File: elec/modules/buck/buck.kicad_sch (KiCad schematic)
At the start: 18 parts, among them J1 Conn_01x08, J2 Conn_01x08, U2 TPS5430DDAG4, U3 TPS5430DDAG4

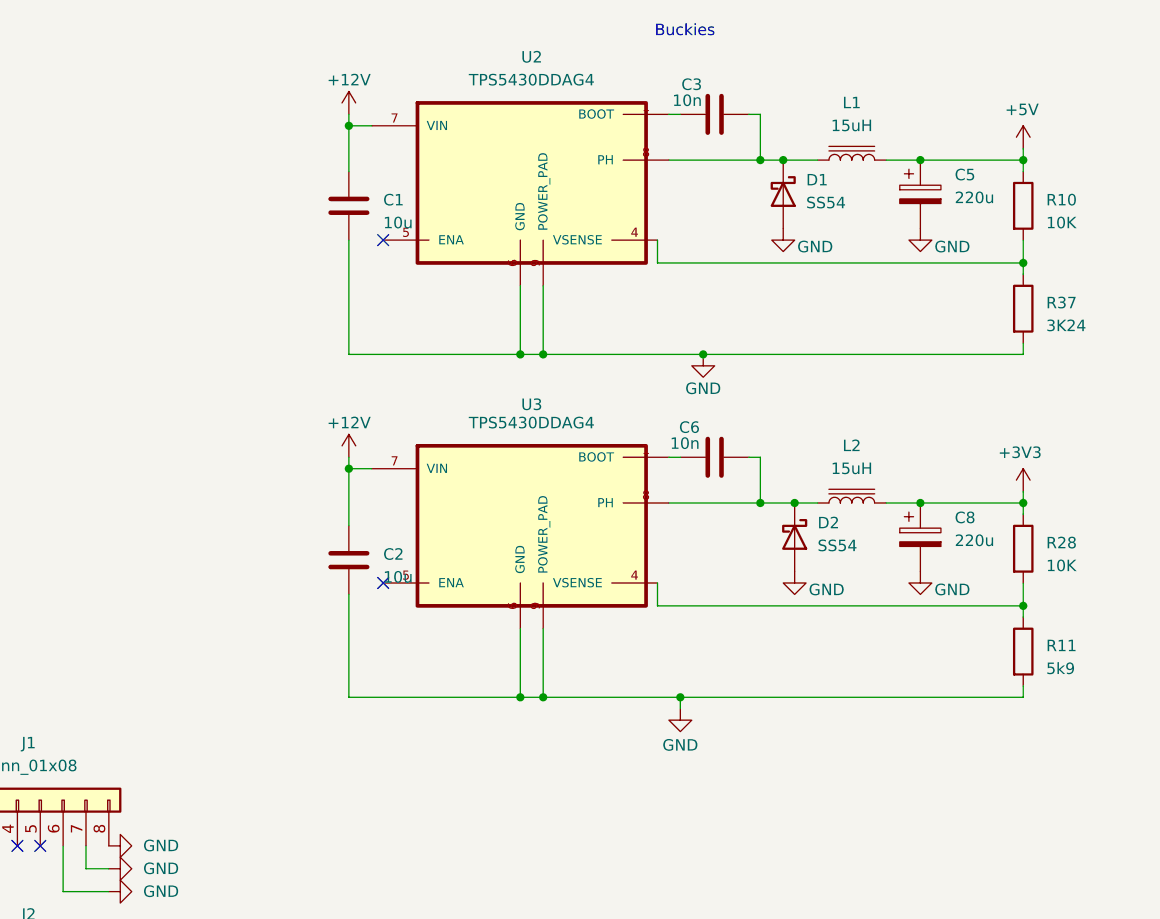
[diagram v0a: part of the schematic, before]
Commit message: Finished slaving avay buck done +PCBA
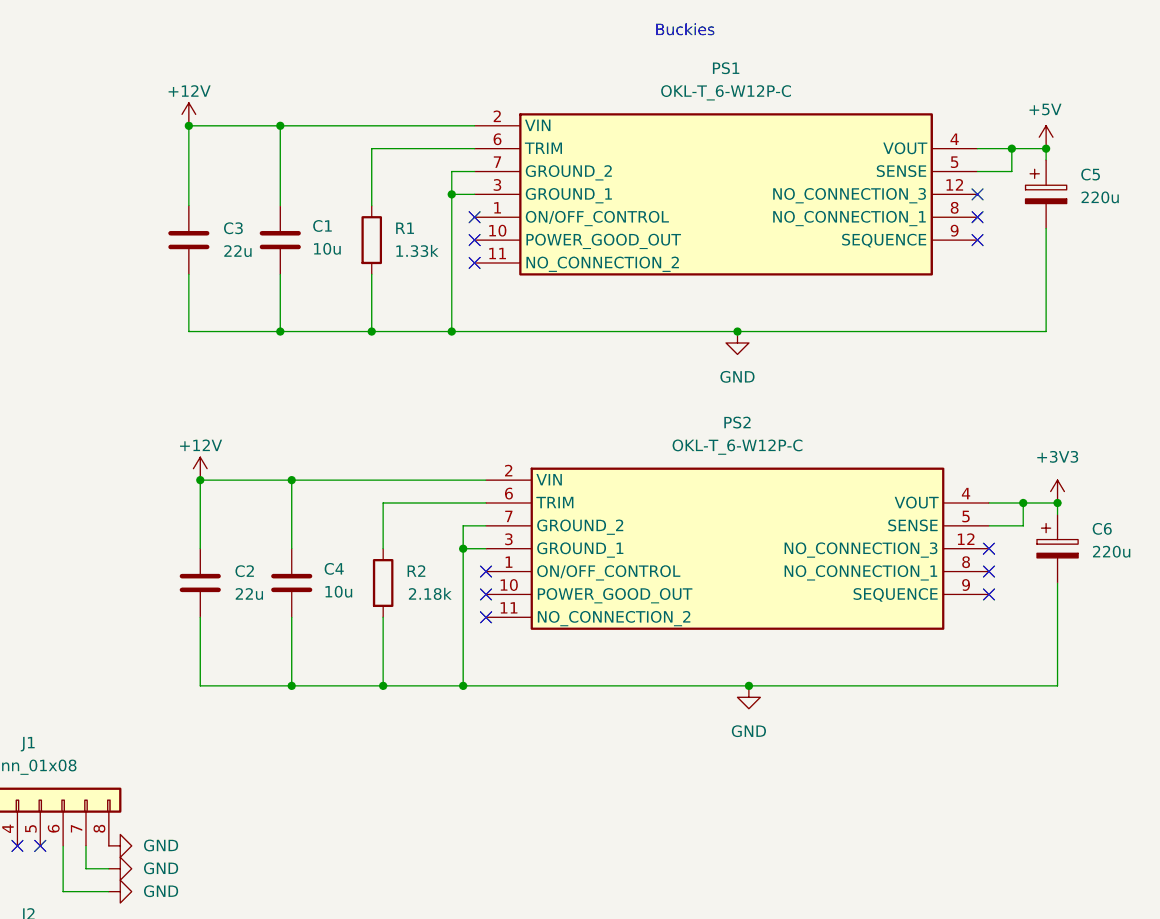
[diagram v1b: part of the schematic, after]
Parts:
- removed C6: 10n, Capacitor_SMD:C_0603_1608Metric, symbol Device:C
- removed C8: 220u, Capacitor_Tantalum_SMD:CP_EIA-7343-15_Kemet-W_HandSolder, symbol Device:C_Polarized
- removed D1, D2: SS54, Buckies:DIOM5025X220N, symbol Diode:B340
- removed L1, L2: 15uH, Buckies:0630 One Piece Inductor, symbol Device:L_Iron
- removed R10, R28: 10K, Resistor_SMD:R_0603_1608Metric, symbol Device:R
- removed R11: 5k9, Resistor_SMD:R_0603_1608Metric, symbol Device:R
- removed R37: 3K24, Resistor_SMD:R_0603_1608Metric, symbol Device:R
- removed U2, U3: TPS5430DDAG4, Buckies:TI_SO-PowerPAD-8, symbol tps5430(buckie):TPS5430DDAG4
- added C4: 10u, Capacitor_SMD:C_0603_1608Metric, symbol Device:C
- added C6: 220u, Capacitor_Tantalum_SMD:CP_EIA-7343-15_Kemet-W_HandSolder, symbol Device:C_Polarized
- added PS1, PS2: OKL-T_6-W12P-C, Buck:OKLT6W12PC, symbol OKL-T/6-W12P-C:OKL-T_6-W12P-C
- added R1: 1.33k, Resistor_SMD:R_0603_1608Metric, symbol Device:R
- added R2: 2.18k, Resistor_SMD:R_0603_1608Metric, symbol Device:R
- C2: value 10u -> 22u
- C3: value 10n -> 22u
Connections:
- net +12V: now also C3.1, C4.1, PS1.2 (VIN), PS2.2 (VIN)
- net +3V3: now also C6.1, PS2.4 (VOUT), PS2.5 (SENSE)
- net +5V: now also PS1.4 (VOUT), PS1.5 (SENSE)
- net GND: now also C3.2, C4.2, C6.2, PS1.3 (GROUND_1), PS1.7 (GROUND_2), PS2.3 (GROUND_1), PS2.7 (GROUND_2), R1.2, R2.2
- new net: PS2.6 (TRIM), R2.1
- new net: PS1.6 (TRIM), R1.1
- no-connect marks 6 -> 16
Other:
- moved on the sheet: C1, C5

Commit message: changed buck footprint
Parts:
- PS1, PS2: footprint Buck:OKLT6W12PC -> Buck:MURATA_OKL-T-6-W12
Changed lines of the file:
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@@
 			)
 		)
-		(property "Footprint" "Buck:OKLT6W12PC"
+		(property "Footprint" "Buck:MURATA_OKL-T-6-W12"
 			(at 156.21 195.25 0)
 			(effects
@@
 			)
 		)
-		(property "Footprint" "Buck:OKLT6W12PC"
+		(property "Footprint" "Buck:MURATA_OKL-T-6-W12"
 			(at 154.94 155.88 0)
 			(effects

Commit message: stuff
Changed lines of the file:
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@@
 	(generator_version "9.0")
 	(paper "A4")
+	(rectangle
+		(start 237.49 90.17)
+		(end 259.715 98.425)
+		(stroke
+			(width 0)
+			(type default)
+		)
+		(fill
+			(type none)
+		)
+	)
+	(rectangle
+		(start 214.63 88.9)
+		(end 232.41 99.06)
+		(stroke
+			(width 0)
+			(type default)
+		)
+		(fill
+			(type none)
+		)
+	)
+	(rectangle
+		(start 209.55 83.82)
+		(end 271.78 119.38)
+		(stroke
+			(width 0)
+			(type default)
+		)
+		(fill
+			(type none)
+		)
+	)
+	(rectangle
+		(start 217.17 111.76)
+		(end 264.16 114.3)
+		(stroke
+			(width 0)
+			(type default)
+		)
+		(fill
+			(type none)
+		)
+	)
 	(text "Buckies"
 		(exclude_from_sim no)

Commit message: Revert "wdicajdfkj,"
This reverts commit e49fd520bb1bff58c9ec61a88596577cb6380b2a.
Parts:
- removed J1, J2: Conn_01x08, Pinheaders:PinHeader_1x08_P2.54mm_Vertical, symbol Connector_Generic:Conn_01x08
- added J1: Conn_01x12, Connector_JST:JST_XH_B12B-XH-AM_1x12_P2.50mm_Vertical, symbol Connector_Generic:Conn_01x12
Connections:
- net +12V: now also J1.4 (Pin_4), J1.5 (Pin_5), J1.6 (Pin_6)
- net +3V3: now also J1.10 (Pin_10), J1.11 (Pin_11), J1.12 (Pin_12)
- net +5V: now also J1.1 (Pin_1), J1.2 (Pin_2), J1.3 (Pin_3)
- net GND: now also J1.7 (Pin_7), J1.8 (Pin_8), J1.9 (Pin_9)
- no-connect marks 16 -> 12

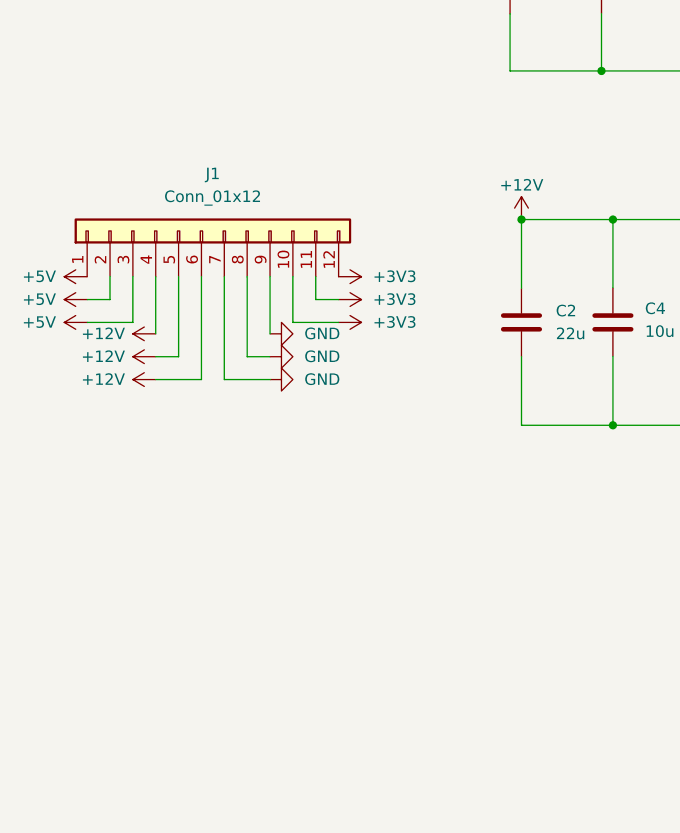
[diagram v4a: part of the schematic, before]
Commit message: Revert "did a bit of buck"
This reverts commit f549f5fa1dabaa1ceabc4869307f1601dc61308a.
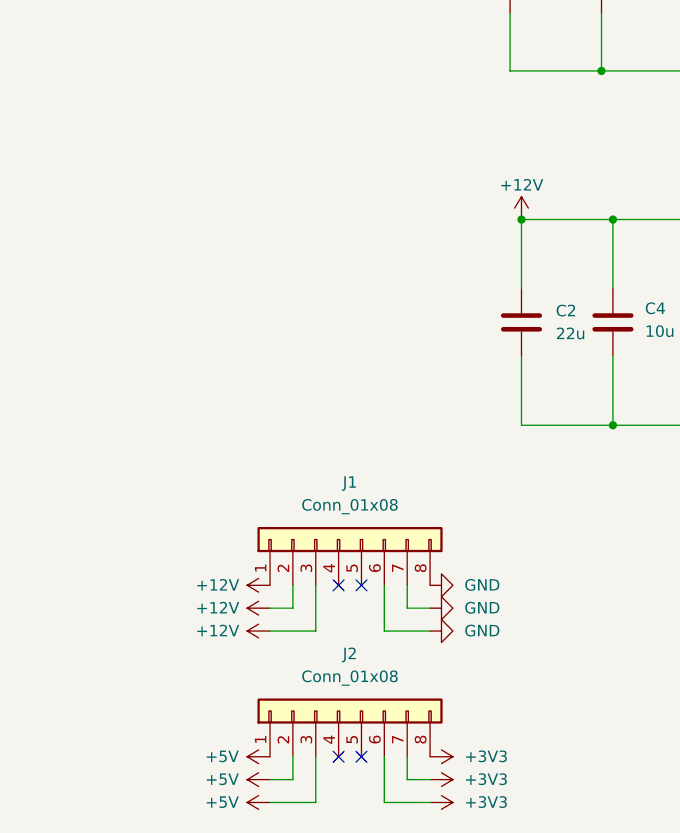
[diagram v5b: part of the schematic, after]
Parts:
- removed J1: Conn_01x12, Connector_JST:JST_XH_B12B-XH-AM_1x12_P2.50mm_Vertical, symbol Connector_Generic:Conn_01x12
- added J1, J2: Conn_01x08, Pinheaders:PinHeader_1x08_P2.54mm_Vertical, symbol Connector_Generic:Conn_01x08
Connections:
- net +12V: now also J1.1 (Pin_1), J1.2 (Pin_2), J1.3 (Pin_3)
- net +3V3: now also J2.6 (Pin_6), J2.7 (Pin_7), J2.8 (Pin_8)
- net +5V: now also J2.1 (Pin_1), J2.2 (Pin_2), J2.3 (Pin_3)
- net GND: now also J1.6 (Pin_6), J1.7 (Pin_7), J1.8 (Pin_8)
- no-connect marks 12 -> 16

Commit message: unfucked bucks and touched on l1/2
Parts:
- added D1, D2: SS54, Buck:DIOM5025X220N, symbol Diode:B340
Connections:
- net +3V3: now also D2.1 (K); no longer C6.1, PS2.4 (VOUT), PS2.5 (SENSE)
- net +5V: now also D1.1 (K); no longer C5.1, PS1.4 (VOUT), PS1.5 (SENSE)
- new net: C5.1, D1.2 (A), PS1.4 (VOUT), PS1.5 (SENSE)
- new net: C6.1, D2.2 (A), PS2.4 (VOUT), PS2.5 (SENSE)
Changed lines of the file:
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@@
 	(generator_version "9.0")
 	(paper "A4")
-	(rectangle
-		(start 237.49 90.17)
-		(end 259.715 98.425)
-		(stroke
-			(width 0)
-			(type default)
-		)
-		(fill
-			(type none)
-		)
-	)
-	(rectangle
-		(start 214.63 88.9)
-		(end 232.41 99.06)
-		(stroke
-			(width 0)
-			(type default)
-		)
-		(fill
-			(type none)
-		)
-	)
-	(rectangle
-		(start 209.55 83.82)
-		(end 271.78 119.38)
-		(stroke
-			(width 0)
-			(type default)
-		)
-		(fill
-			(type none)
-		)
-	)
-	(rectangle
-		(start 217.17 111.76)
-		(end 264.16 114.3)
-		(stroke
-			(width 0)
-			(type default)
-		)
-		(fill
-			(type none)
-		)
-	)
 	(text "Buckies"
 		(exclude_from_sim no)
@@
 	(wire
 		(pts
+			(xy 179.07 62.23) (xy 177.8 62.23)
+		)
+		(stroke
+			(width 0)
+			(type default)
+		)
+	)
+	(wire
+		(pts
 			(xy 81.28 59.69) (xy 102.87 59.69)
 		)
@@
 	(wire
 		(pts
+			(xy 179.07 101.6) (xy 177.8 101.6)
+		)
+		(stroke
+			(width 0)
+			(type default)
+		)
+	)
+	(wire
+		(pts
 			(xy 162.56 64.77) (xy 162.56 62.23)
 		)
@@
 	(wire
 		(pts
+			(xy 170.18 101.6) (xy 167.64 101.6)
+		)
+		(stroke
+			(width 0)
+			(type default)
+		)
+	)
+	(wire
+		(pts
 			(xy 46.99 158.75) (xy 46.99 161.29)
 		)
@@
 		(pts
 			(xy 104.14 104.14) (xy 101.6 104.14)
+		)
+		(stroke
+			(width 0)
+			(type default)
+		)
+	)
+	(wire
+		(pts
+			(xy 170.18 62.23) (xy 166.37 62.23)
 		)
 		(stroke
@@
 	(symbol
 		(lib_id "power:+3V3")
-		(at 167.64 101.6 0)
+		(at 179.07 101.6 270)
 		(unit 1)
 		(exclude_from_sim no)
@@
 		(fields_autoplaced yes)
 		(property "Reference" "#PWR012"
-			(at 167.64 105.41 0)
+			(at 175.26 101.6 0)
 			(effects
 				(font
@@
 		)
 		(property "Value" "+3V3"
-			(at 167.64 96.52 0)
-			(effects
-				(font
-					(size 1.27 1.27)
-				)
+			(at 182.88 101.5999 90)
+			(effects
+				(font
+					(size 1.27 1.27)
+				)
+				(justify left)
 			)
 		)
 		(property "Footprint" ""
-			(at 167.64 101.6 0)
+			(at 179.07 101.6 0)
 			(effects
 				(font
@@
 		)
 		(property "Datasheet" ""
-			(at 167.64 101.6 0)
+			(at 179.07 101.6 0)
 			(effects
 				(font
@@
 		)
 		(property "Description" "Power symbol creates a global label with name \"+3V3\""
-			(at 167.64 101.6 0)
+			(at 179.07 101.6 0)
 			(effects
 				(font
@@
 	)
 	(symbol
+		(lib_id "Diode:B340")
+		(at 173.99 62.23 180)
+		(unit 1)
+		(exclude_from_sim no)
+		(in_bom yes)
+		(on_board yes)
+		(dnp no)
+		(fields_autoplaced yes)
+		(property "Reference" "D1"
+			(at 174.3075 55.88 0)
+			(effects
+				(font
+					(size 1.27 1.27)
+				)
+			)
+		)
+		(property "Value" "SS54"
+			(at 174.3075 58.42 0)
+			(effects
+				(font
+					(size 1.27 1.27)
+				)
+			)
+		)
+		(property "Footprint" "Buck:DIOM5025X220N"
+			(at 173.99 57.785 0)
+			(effects
+				(font
+					(size 1.27 1.27)
+				)
+				(hide yes)
+			)
+		)
+		(property "Datasheet" "http://www.jameco.com/Jameco/Products/ProdDS/1538777.pdf"
+			(at 173.99 62.23 0)
+			(effects
+				(font
+					(size 1.27 1.27)
+				)
+				(hide yes)
+			)
+		)
+		(property "Description" ""
+			(at 173.99 62.23 0)
+			(effects
+				(font
+					(size 1.27 1.27)
+				)
+				(hide yes)
+			)
+		)
+		(pin "1"
+		)
+		(pin "2"
+		)
+		(instances
+			(project "buck"
+				(path "/b0c14512-e8a3-4c13-88d8-be98af63a21a"
+					(reference "D1")
+					(unit 1)
+				)
+			)
+		)
+	)
+	(symbol
 		(lib_id "power:+3V3")
 		(at 62.23 158.75 270)
@@
 	)
 	(symbol
+		(lib_id "Diode:B340")
+		(at 173.99 101.6 180)
+		(unit 1)
+		(exclude_from_sim no)
+		(in_bom yes)
+		(on_board yes)
+		(dnp no)
+		(fields_autoplaced yes)
+		(property "Reference" "D2"
+			(at 174.3075 95.25 0)
+			(effects
+				(font
+					(size 1.27 1.27)
+				)
+			)
+		)
+		(property "Value" "SS54"
+			(at 174.3075 97.79 0)
+			(effects
+				(font
+					(size 1.27 1.27)
+				)
+			)
+		)
+		(property "Footprint" "Buck:DIOM5025X220N"
+			(at 173.99 97.155 0)
+			(effects
+				(font
+					(size 1.27 1.27)
+				)
+				(hide yes)
+			)
+		)
+		(property "Datasheet" "http://www.jameco.com/Jameco/Products/ProdDS/1538777.pdf"
+			(at 173.99 101.6 0)
+			(effects
+				(font
+					(size 1.27 1.27)
+				)
+				(hide yes)
+			)
+		)
+		(property "Description" ""
+			(at 173.99 101.6 0)
+			(effects
+				(font
+					(size 1.27 1.27)
+				)
+				(hide yes)
+			)
+		)
+		(pin "1"
+		)
+		(pin "2"
+		)
+		(instances
+			(project "buck"
+				(path "/b0c14512-e8a3-4c13-88d8-be98af63a21a"
+					(reference "D2")
+					(unit 1)
+				)
+			)
+		)
+	)
+	(symbol
 		(lib_id "Device:C_Polarized")
 		(at 167.64 106.68 0)
@@
 	(symbol
 		(lib_id "power:+5V")
-		(at 166.37 62.23 0)
+		(at 179.07 62.23 270)
 		(unit 1)
 		(exclude_from_sim no)
@@
 		(dnp no)
 		(property "Reference" "#PWR025"
-			(at 166.37 66.04 0)
+			(at 175.26 62.23 0)
 			(effects
 				(font
@@
 		)
 		(property "Value" "+5V"
-			(at 164.338 57.912 0)
+			(at 183.388 60.198 0)
 			(effects
 				(font
@@
 		)
 		(property "Footprint" ""
-			(at 166.37 62.23 0)
+			(at 179.07 62.23 0)
 			(effects
 				(font
@@
 		)
 		(property "Datasheet" ""
-			(at 166.37 62.23 0)
+			(at 179.07 62.23 0)
 			(effects
 				(font
@@
 		)
 		(property "Description" "Power symbol creates a global label with name \"+5V\""
-			(at 166.37 62.23 0)
-			(effects
-				(font
+			(at 179.07 62.23 0)
+			(effects
+				(font
